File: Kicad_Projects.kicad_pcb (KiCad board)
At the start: 2 copper layers, 100.3 x 50.8 mm, 30 parts, among them J1 Ent. 15Vca, J2 Vcc_Volt/Amper, J3 Vout, J4 Amperimetro, Q1 BD137, Q2 TIP3055G, U1 LM723_DIP14

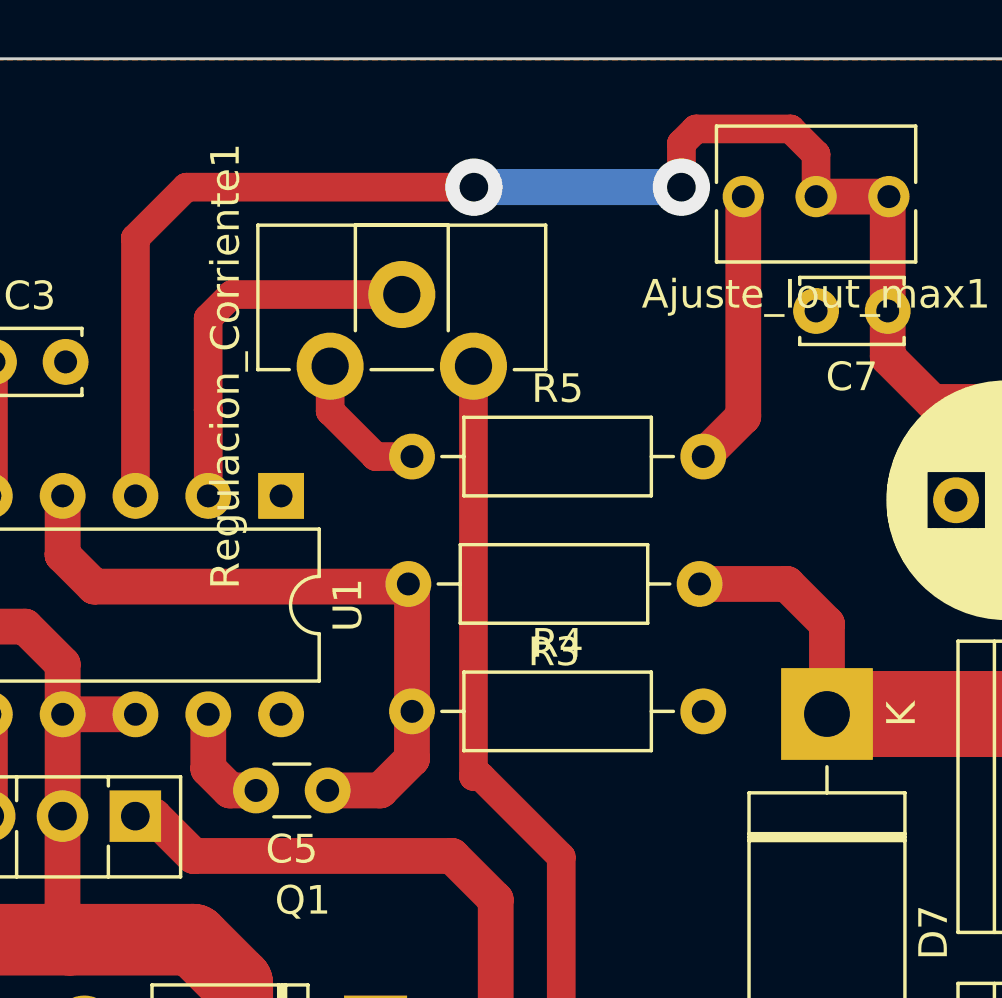
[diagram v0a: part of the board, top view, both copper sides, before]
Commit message: cambio jumper y BOM en .csv
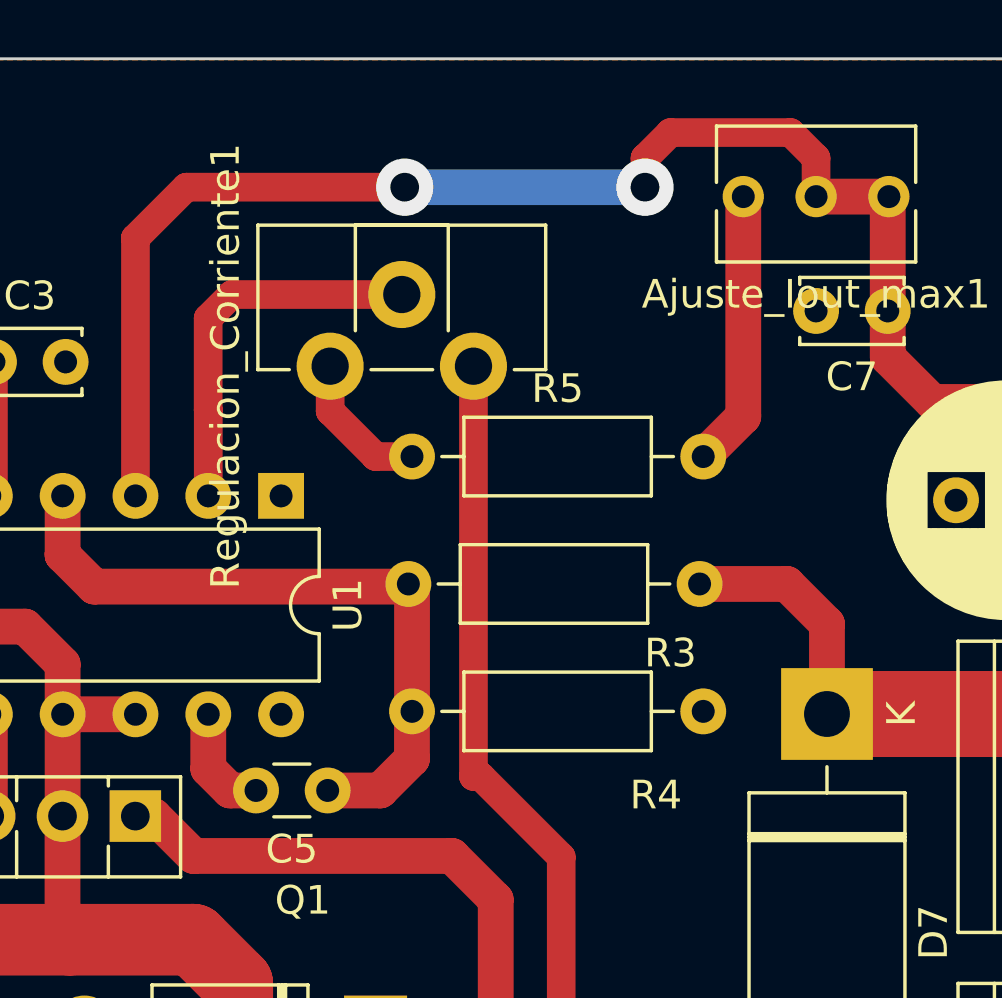
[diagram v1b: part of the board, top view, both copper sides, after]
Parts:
- R2: value 2k2 -> 1k8
- R3: value 2K7 -> 1K8

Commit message: PCB y gerbers actualizado
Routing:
- net TBJ_Out: track 84.8 -> 87.1 mm
- net AC_F: track 42.8 -> 43.8 mm
- added copper zone on B.Cu, net GND
- removed copper zone on F.Cu, net GND

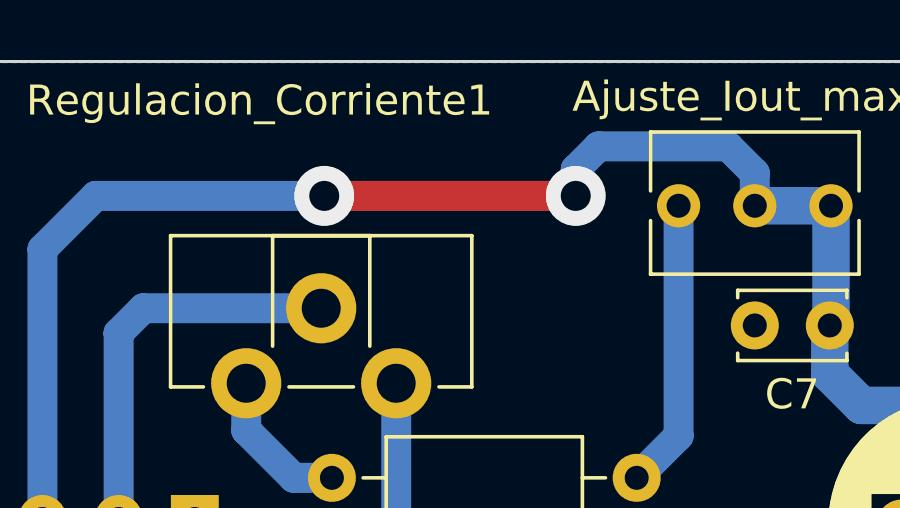
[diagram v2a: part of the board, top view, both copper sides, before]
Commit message: agregado en F_silk jumper
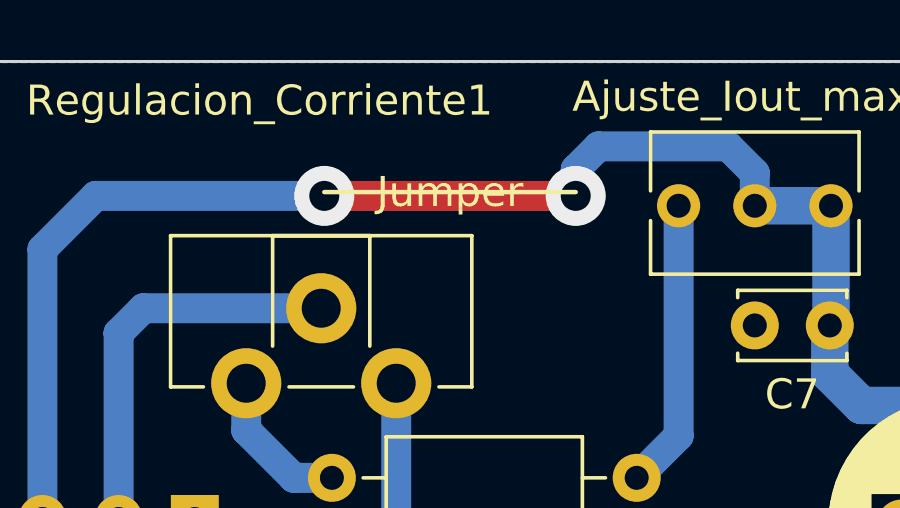
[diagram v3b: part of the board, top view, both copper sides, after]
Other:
- board text added: "Jumper"
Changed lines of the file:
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@@
     )
   )
+  (gr_line (start 136.653 76.743) (end 145.035 76.743) (layer "F.SilkS") (width 0.15))
   (gr_line (start 63.5 72.39) (end 63.5 123.19) (layer "Edge.Cuts") (width 0.1))
   (gr_line (start 163.83 123.19) (end 163.83 72.39) (layer "Edge.Cuts") (width 0.1))
@@
     (effects (font (size 1.5 1.5) (thickness 0.3)))
   )
+  (gr_text "Jumper" (at 140.844 76.743) (layer "F.SilkS")
+    (effects (font (size 1 1) (thickness 0.15)))
+  )
   (gr_text "Fuente 18V 3A\nMecatronica 1 -FRC- UTN" (at 80.265 74.711) (layer "F.SilkS")
